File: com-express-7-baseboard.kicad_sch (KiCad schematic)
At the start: 0 parts

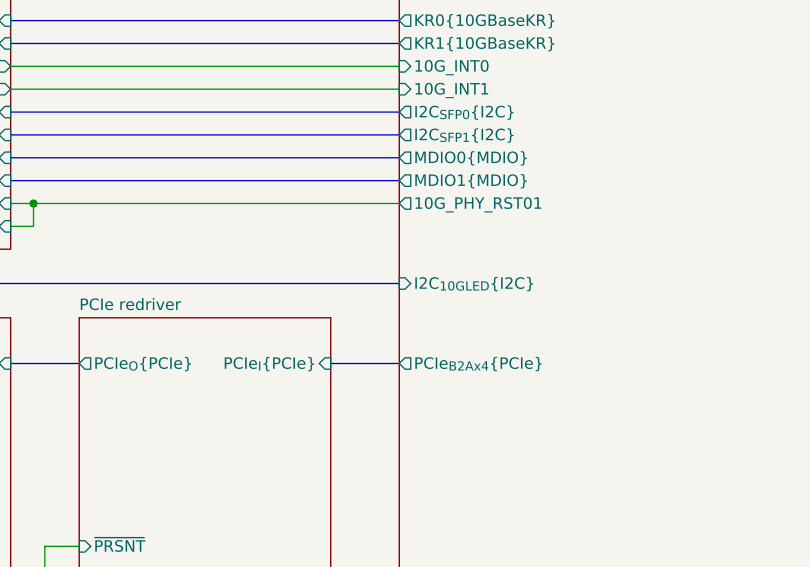
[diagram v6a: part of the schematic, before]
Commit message: [#57905] Add carrier board EEPROM
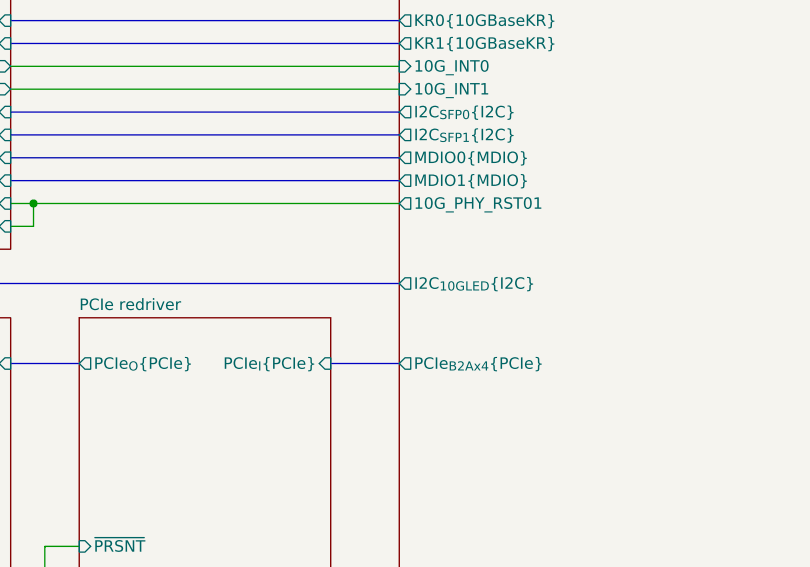
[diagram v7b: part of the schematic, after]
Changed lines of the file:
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@@
       (effects (font (size 1.27 1.27)) (justify left))
     )
-    (pin "I2C_{10GLED}{I2C}" input (at 162.56 135.89 180)
+    (pin "I2C_{10GLED}{I2C}" output (at 162.56 135.89 180)
       (effects (font (size 1.27 1.27)) (justify left))
     )

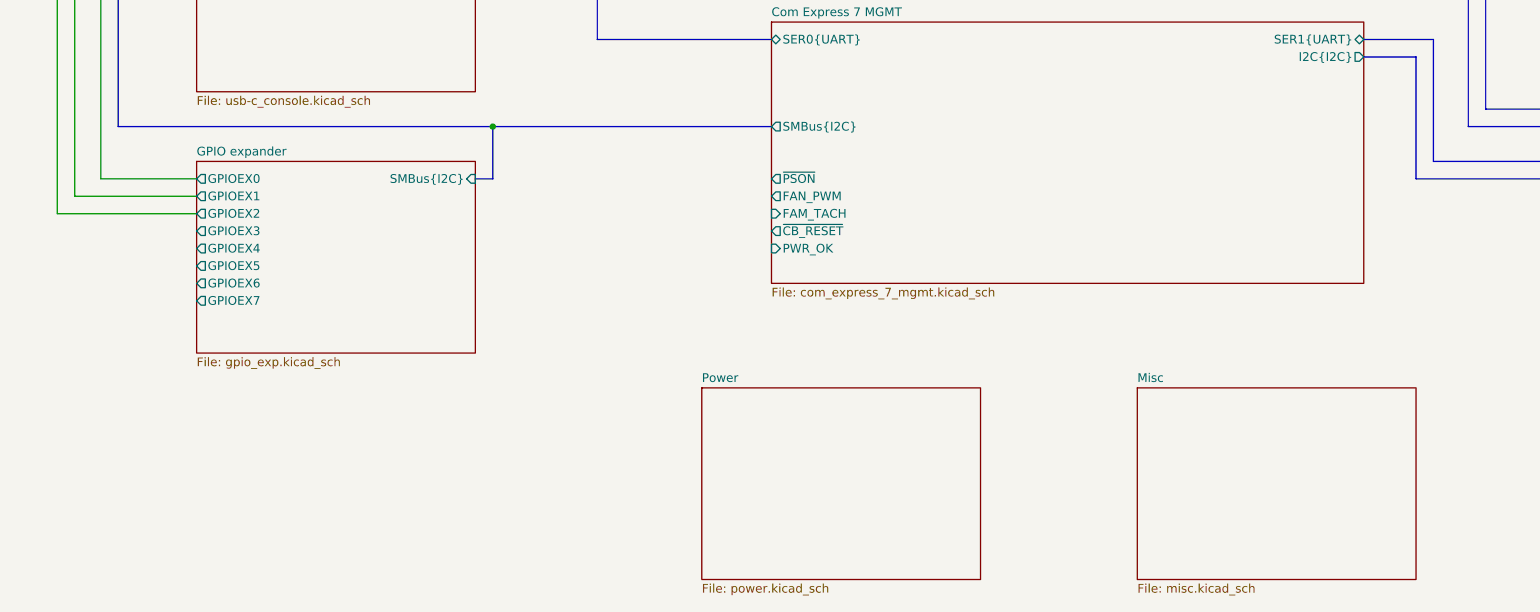
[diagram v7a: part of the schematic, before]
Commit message: [#57905] Add ADT7476AARQZ temperature/voltage/fan system monitor, LEDs
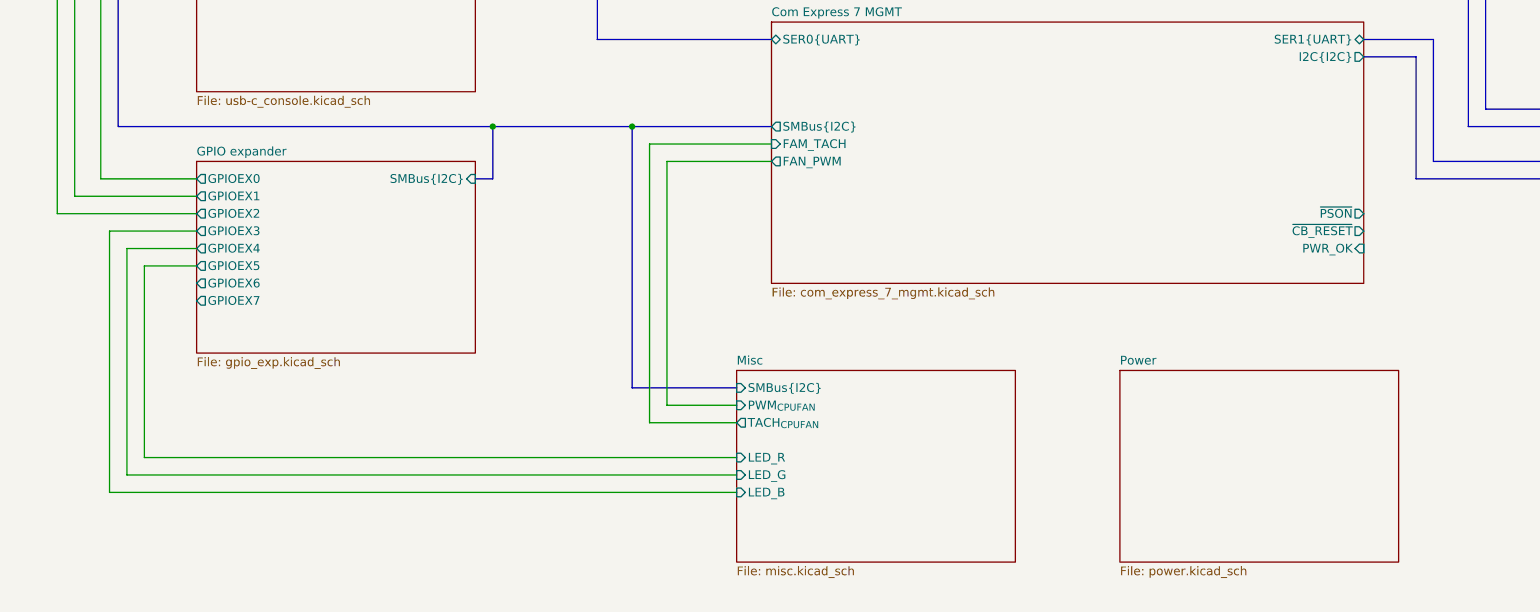
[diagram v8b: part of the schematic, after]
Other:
- sheet Misc ports: added LED_B, LED_G, LED_R, PWM_{CPUFAN}, SMBus{I2C}, TACH_{CPUFAN}; removed none
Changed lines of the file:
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@@
   (junction (at 325.12 101.6) (diameter 0) (color 0 0 0 0)
+  )
+  (junction (at 142.24 208.28) (diameter 0) (color 0 0 0 0)
   )
   (junction (at 64.77 171.45) (diameter 0) (color 0 0 0 0)
@@
     (stroke (width 0) (type default))
   )
+  (wire (pts (xy 78.74 223.52) (xy 66.04 223.52))
+    (stroke (width 0) (type default))
+  )
   (bus (pts (xy 335.28 106.68) (xy 335.28 27.94))
     (stroke (width 0) (type default))
@@
   )
   (wire (pts (xy 270.51 173.99) (xy 270.51 168.91))
+    (stroke (width 0) (type default))
+  )
+  (wire (pts (xy 71.12 256.54) (xy 71.12 228.6))
     (stroke (width 0) (type default))
   )
@@
     (stroke (width 0) (type default) (color 255 153 0 1))
   )
+  (wire (pts (xy 144.78 251.46) (xy 157.48 251.46))
+    (stroke (width 0) (type default))
+  )
   (bus (pts (xy 248.92 175.26) (xy 252.73 175.26))
     (stroke (width 0) (type default) (color 0 255 255 1))
@@
     (stroke (width 0) (type default))
   )
+  (wire (pts (xy 71.12 228.6) (xy 78.74 228.6))
+    (stroke (width 0) (type default))
+  )
   (bus (pts (xy 299.72 30.48) (xy 332.74 30.48))
     (stroke (width 0) (type default))
@@
     (stroke (width 0) (type default))
   )
+  (wire (pts (xy 157.48 248.92) (xy 147.32 248.92))
+    (stroke (width 0) (type default))
+  )
   (bus (pts (xy 119.38 81.28) (xy 162.56 81.28))
     (stroke (width 0) (type default) (color 0 0 255 1))
@@
     (stroke (width 0) (type default))
   )
+  (wire (pts (xy 66.04 223.52) (xy 66.04 261.62))
+    (stroke (width 0) (type default))
+  )
+  (wire (pts (xy 66.04 261.62) (xy 157.48 261.62))
+    (stroke (width 0) (type default))
+  )
   (wire (pts (xy 322.58 101.6) (xy 325.12 101.6))
+    (stroke (width 0) (type default))
+  )
+  (bus (pts (xy 157.48 246.38) (xy 142.24 246.38))
     (stroke (width 0) (type default))
   )
@@
     (stroke (width 0) (type default))
   )
+  (wire (pts (xy 157.48 259.08) (xy 68.58 259.08))
+    (stroke (width 0) (type default))
+  )
   (wire (pts (xy 58.42 66.04) (xy 58.42 220.98))
     (stroke (width 0) (type default))
@@
     (stroke (width 0) (type default))
   )
-  (bus (pts (xy 121.92 208.28) (xy 162.56 208.28))
+  (wire (pts (xy 157.48 256.54) (xy 71.12 256.54))
+    (stroke (width 0) (type default))
+  )
+  (bus (pts (xy 121.92 208.28) (xy 142.24 208.28))
     (stroke (width 0) (type default))
   )
   (wire (pts (xy 327.66 139.7) (xy 327.66 104.14))
+    (stroke (width 0) (type default))
+  )
+  (bus (pts (xy 142.24 208.28) (xy 162.56 208.28))
+    (stroke (width 0) (type default))
+  )
+  (wire (pts (xy 147.32 213.36) (xy 162.56 213.36))
     (stroke (width 0) (type default))
   )
@@
     (stroke (width 0) (type default))
   )
+  (wire (pts (xy 147.32 248.92) (xy 147.32 213.36))
+    (stroke (width 0) (type default))
+  )
+  (wire (pts (xy 162.56 210.82) (xy 144.78 210.82))
+    (stroke (width 0) (type default))
+  )
   (bus (pts (xy 119.38 124.46) (xy 162.56 124.46))
     (stroke (width 0) (type default))
@@
     (stroke (width 0) (type default))
   )
+  (wire (pts (xy 68.58 259.08) (xy 68.58 226.06))
+    (stroke (width 0) (type default))
+  )
   (bus (pts (xy 254 35.56) (xy 261.62 35.56))
     (stroke (width 0) (type default))
@@
     (stroke (width 0) (type default))
   )
+  (bus (pts (xy 142.24 246.38) (xy 142.24 208.28))
+    (stroke (width 0) (type default))
+  )
   (bus (pts (xy 78.74 129.54) (xy 76.2 129.54))
+    (stroke (width 0) (type default))
+  )
+  (wire (pts (xy 68.58 226.06) (xy 78.74 226.06))
     (stroke (width 0) (type default))
   )
@@
     (stroke (width 0) (type default) (color 194 0 194 1))
   )
+  (wire (pts (xy 144.78 210.82) (xy 144.78 251.46))
+    (stroke (width 0) (type default))
+  )
   (wire (pts (xy 78.74 220.98) (xy 58.42 220.98))
     (stroke (width 0) (type default))
@@
     )
   )
-  (sheet (at 215.9 246.38) (size 40.64 27.94) (fields_autoplaced)
-    (stroke (width 0.1524) (type solid))
-    (fill (color 0 0 0 0.0000))
-    (property "Sheetname" "Misc" (at 215.9 245.6684 0)
-      (effects (font (size 1.27 1.27)) (justify left bottom))
-    )
-    (property "Sheetfile" "misc.kicad_sch" (at 215.9 274.9046 0)
-      (effects (font (size 1.27 1.27)) (justify left top))
+  (sheet (at 157.48 243.84) (size 40.64 27.94) (fields_autoplaced)
+    (stroke (width 0.1524) (type solid))
+    (fill (color 0 0 0 0.0000))
+    (property "Sheetname" "Misc" (at 157.48 243.1284 0)
+      (effects (font (size 1.27 1.27)) (justify left bottom))
+    )
+    (property "Sheetfile" "misc.kicad_sch" (at 157.48 272.3646 0)
+      (effects (font (size 1.27 1.27)) (justify left top))
+    )
+    (pin "TACH_{CPUFAN}" output (at 157.48 251.46 180)
+      (effects (font (size 1.27 1.27)) (justify left))
+    )
+    (pin "PWM_{CPUFAN}" input (at 157.48 248.92 180)
+      (effects (font (size 1.27 1.27)) (justify left))
+    )
+    (pin "SMBus{I2C}" input (at 157.48 246.38 180)
+      (effects (font (size 1.27 1.27)) (justify left))
+    )
+    (pin "LED_G" input (at 157.48 259.08 180)
+      (effects (font (size 1.27 1.27)) (justify left))
+    )
+    (pin "LED_B" input (at 157.48 261.62 180)
+      (effects (font (size 1.27 1.27)) (justify left))
+    )
+    (pin "LED_R" input (at 157.48 256.54 180)
+      (effects (font (size 1.27 1.27)) (justify left))
     )
     (instances
@@
     )
   )
-  (sheet (at 152.4 246.38) (size 40.64 27.94) (fields_autoplaced)
-    (stroke (width 0.1524) (type solid))
-    (fill (color 0 0 0 0.0000))
-    (property "Sheetname" "Power" (at 152.4 245.6684 0)
-      (effects (font (size 1.27 1.27)) (justify left bottom))
-    )
-    (property "Sheetfile" "power.kicad_sch" (at 152.4 274.9046 0)
+  (sheet (at 213.36 243.84) (size 40.64 27.94) (fields_autoplaced)
+    (stroke (width 0.1524) (type solid))
+    (fill (color 0 0 0 0.0000))
+    (property "Sheetname" "Power" (at 213.36 243.1284 0)
+      (effects (font (size 1.27 1.27)) (justify left bottom))
+    )
+    (property "Sheetfile" "power.kicad_sch" (at 213.36 272.3646 0)
       (effects (font (size 1.27 1.27)) (justify left top))
     )
@@
       (effects (font (size 1.27 1.27)) (justify left))
     )
-    (pin "~{PSON}" output (at 162.56 215.9 180)
-      (effects (font (size 1.27 1.27)) (justify left))
-    )
-    (pin "FAN_PWM" output (at 162.56 218.44 180)
-      (effects (font (size 1.27 1.27)) (justify left))
-    )
-    (pin "FAM_TACH" input (at 162.56 220.98 180)
-      (effects (font (size 1.27 1.27)) (justify left))
-    )
-    (pin "~{CB_RESET}" output (at 162.56 223.52 180)
-      (effects (font (size 1.27 1.27)) (justify left))
-    )
-    (pin "PWR_OK" input (at 162.56 226.06 180)
-      (effects (font (size 1.27 1.27)) (justify left))
+    (pin "~{PSON}" output (at 248.92 220.98 0)
+      (effects (font (size 1.27 1.27)) (justify right))
+    )
+    (pin "FAN_PWM" output (at 162.56 213.36 180)
+      (effects (font (size 1.27 1.27)) (justify left))
+    )
+    (pin "FAM_TACH" input (at 162.56 210.82 180)
+      (effects (font (size 1.27 1.27)) (justify left))
+    )
+    (pin "~{CB_RESET}" output (at 248.92 223.52 0)
+      (effects (font (size 1.27 1.27)) (justify right))
+    )
+    (pin "PWR_OK" input (at 248.92 226.06 0)
+      (effects (font (size 1.27 1.27)) (justify right))
     )
     (pin "I2C{I2C}" output (at 248.92 198.12 0)
